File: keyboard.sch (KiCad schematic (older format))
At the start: 16 parts, among them SW1 SW_Push, U1 ATmega32U4-AU, Y1 16MHz

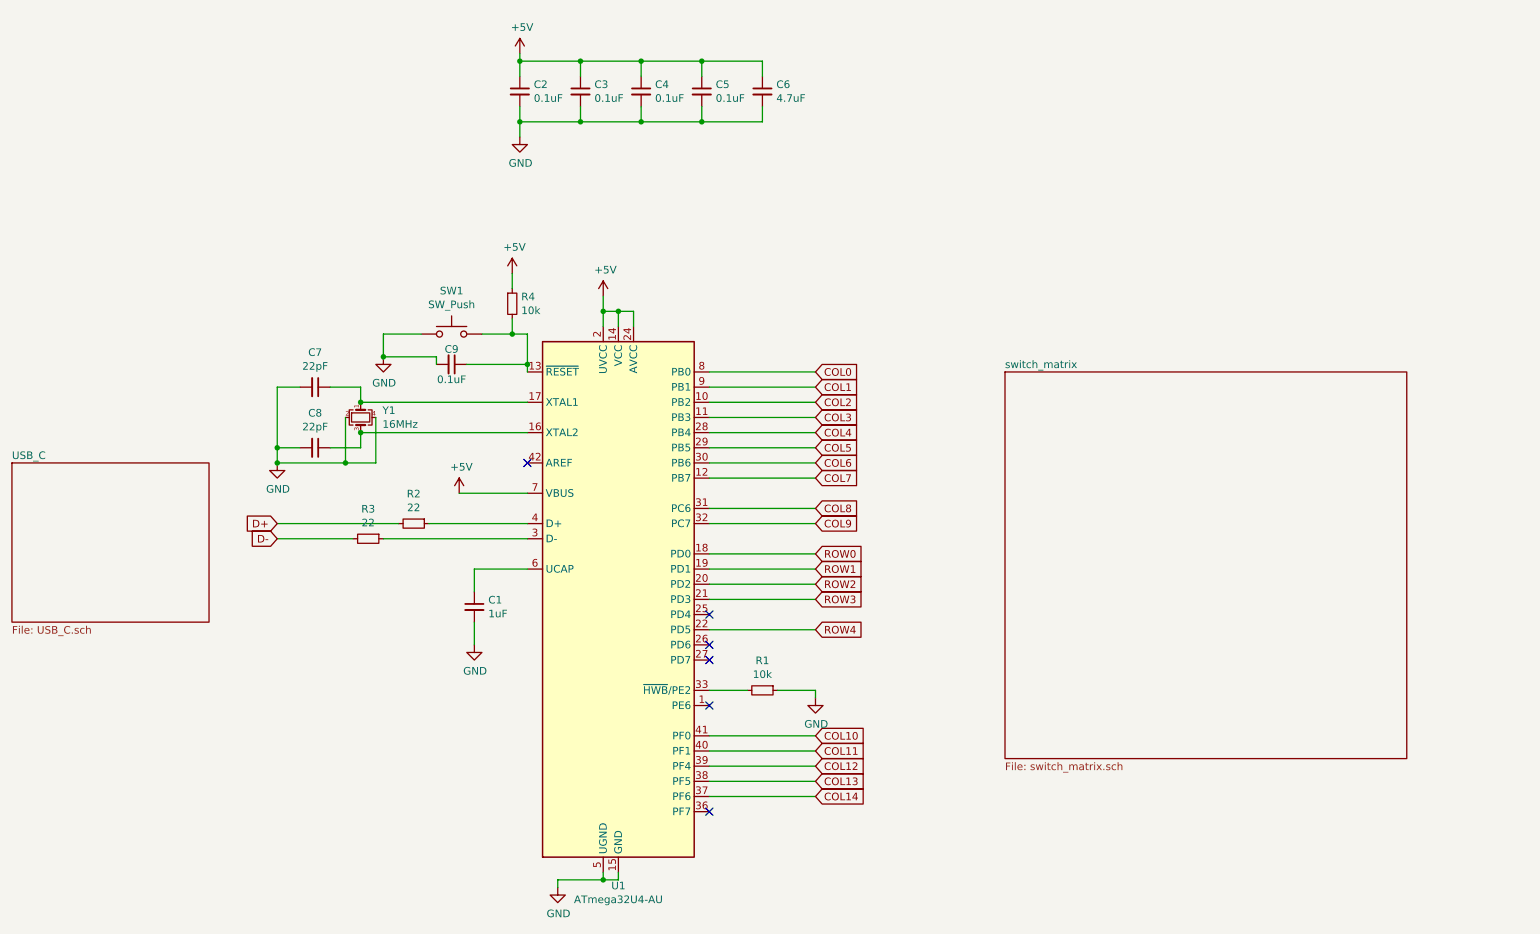
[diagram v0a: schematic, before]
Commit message: Assigned footprint
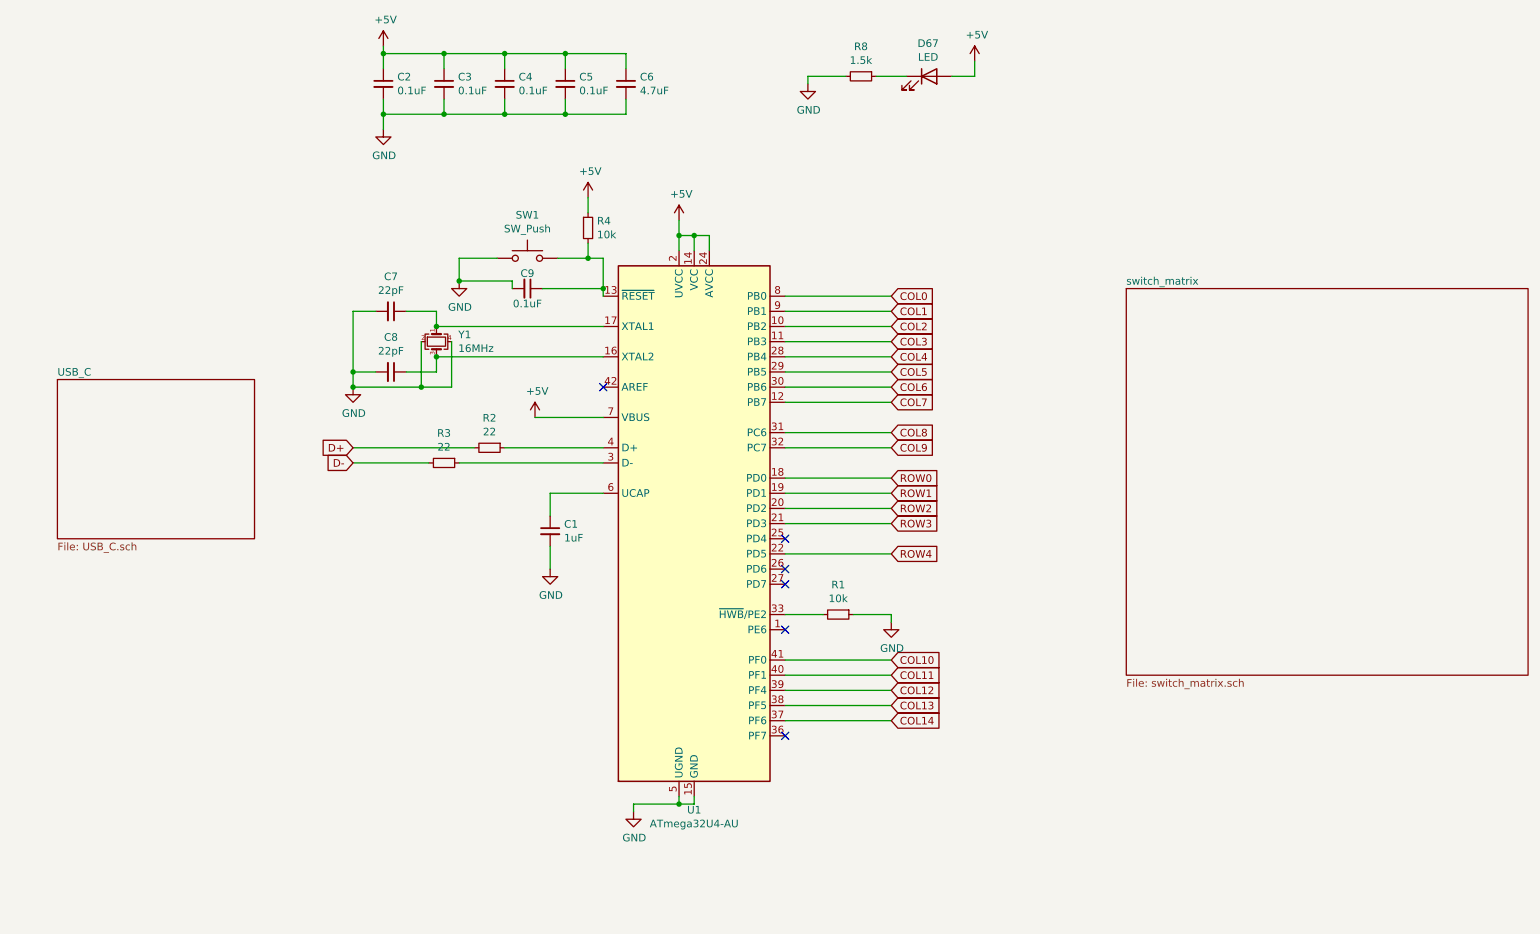
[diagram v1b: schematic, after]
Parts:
- added D67: LED, LED_SMD:LED_0805_2012Metric, symbol Device:LED
- added R8: 1.5k, Resistor_SMD:R_0805_2012Metric, symbol Device:R_Small
- C1, C2, C3, C4, C5, C6, C7, C8, C9: footprint (none) -> Capacitor_SMD:C_0805_2012Metric
- R1, R2, R3, R4: footprint (none) -> Resistor_SMD:R_0805_2012Metric
- SW1: footprint (none) -> random-keyboard-parts:SKQG-1155865
- Y1: footprint (none) -> Crystal:Crystal_SMD_3225-4Pin_3.2x2.5mm
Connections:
- net +5V: now also D67.2 (A)
- net GND: now also R8.2
- new net: D67.1 (K), R8.1
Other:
- moved on the sheet: C1, C2, C3, C4, C5, C6, C7, C8, C9, R1, R2, R3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

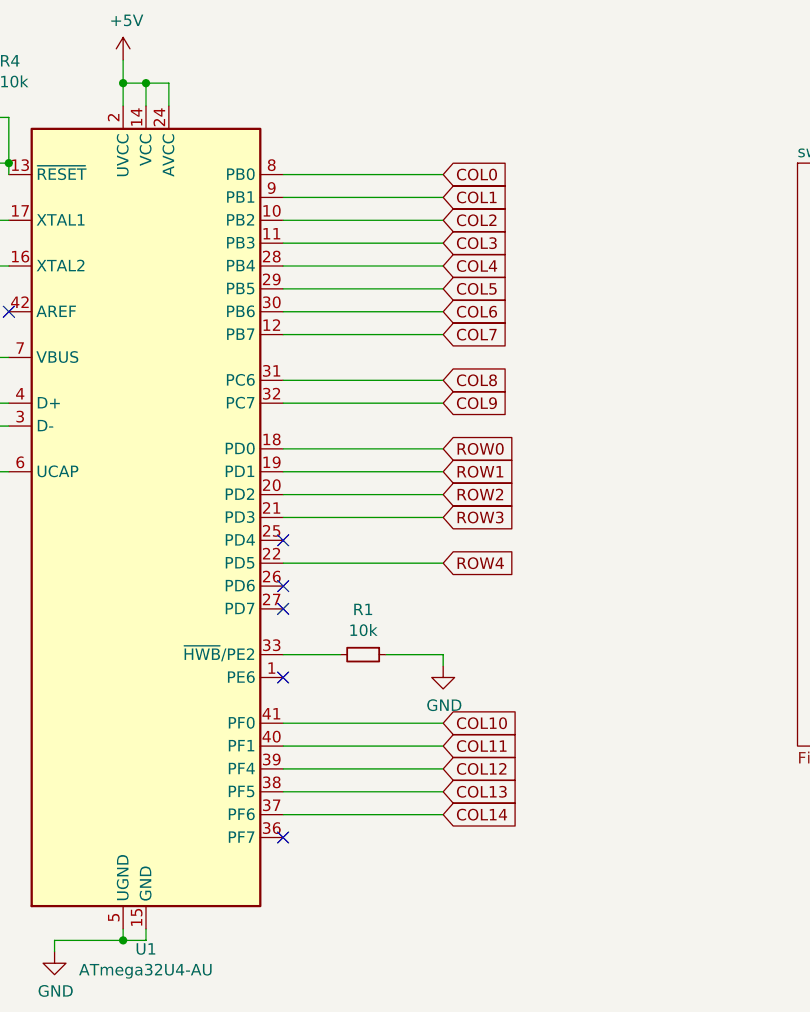
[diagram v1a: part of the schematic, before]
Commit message: Finished routing, filled in ground planes, checked with DRC and 3D render
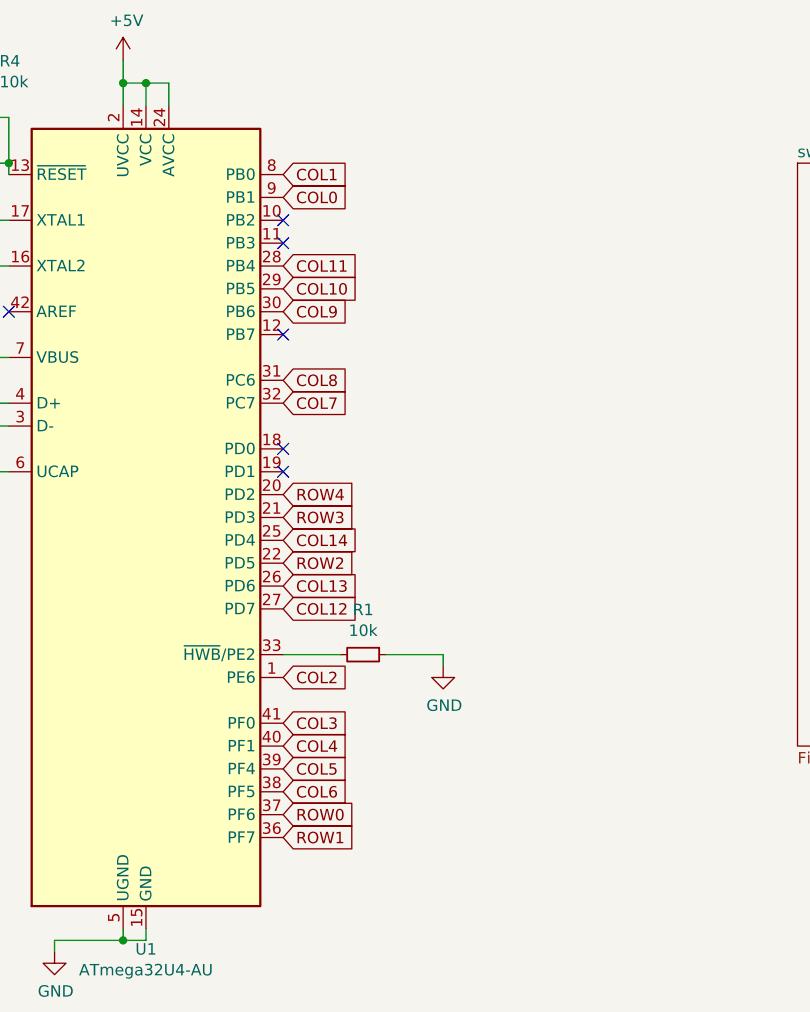
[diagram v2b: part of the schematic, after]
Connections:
- net COL0: now also U1.9 (PB1); no longer U1.8 (PB0)
- net COL1: now also U1.8 (PB0); no longer U1.9 (PB1)
- net COL10: now also U1.29 (PB5); no longer U1.41 (PF0)
- net COL11: now also U1.28 (PB4); no longer U1.40 (PF1)
- net COL12: now also U1.27 (PD7); no longer U1.39 (PF4)
- net COL13: now also U1.26 (PD6); no longer U1.38 (PF5)
- net COL14: now also U1.25 (PD4); no longer U1.37 (PF6)
- net COL2: now also U1.1 (PE6); no longer U1.10 (PB2)
- net COL3: now also U1.41 (PF0); no longer U1.11 (PB3)
- net COL4: now also U1.40 (PF1); no longer U1.28 (PB4)
- net COL5: now also U1.39 (PF4); no longer U1.29 (PB5)
- net COL6: now also U1.38 (PF5); no longer U1.30 (PB6)
- net COL7: now also U1.32 (PC7); no longer U1.12 (PB7)
- net COL9: now also U1.30 (PB6); no longer U1.32 (PC7)
- net ROW0: now also U1.37 (PF6); no longer U1.18 (PD0)
- net ROW1: now also U1.36 (PF7); no longer U1.19 (PD1)
- net ROW2: now also U1.22 (PD5); no longer U1.20 (PD2)
- net ROW4: now also U1.20 (PD2); no longer U1.22 (PD5)
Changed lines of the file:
@@
 	5350 2250 5350 2350
 Connection ~ 5250 2250
-Wire Wire Line
-	5850 3850 6550 3850
-Wire Wire Line
-	5850 3950 6550 3950
-Wire Wire Line
-	5850 4050 6550 4050
-Wire Wire Line
-	5850 4150 6550 4150
-Wire Wire Line
-	5850 4350 6550 4350
-Text GLabel 6550 3850 2    50   Input ~ 0
+Text GLabel 5850 5450 2    50   Input ~ 0
 ROW0
-Text GLabel 6550 3950 2    50   Input ~ 0
+Text GLabel 5850 5550 2    50   Input ~ 0
 ROW1
-Text GLabel 6550 4050 2    50   Input ~ 0
+Text GLabel 5850 4350 2    50   Input ~ 0
 ROW2
-Text GLabel 6550 4150 2    50   Input ~ 0
+Text GLabel 5850 4150 2    50   Input ~ 0
 ROW3
-Text GLabel 6550 4350 2    50   Input ~ 0
+Text GLabel 5850 4050 2    50   Input ~ 0
 ROW4
-Wire Wire Line
-	5850 2650 6550 2650
-Wire Wire Line
-	5850 2750 6550 2750
-Wire Wire Line
-	5850 2850 6550 2850
-Wire Wire Line
-	5850 2950 6550 2950
-Wire Wire Line
-	5850 3050 6550 3050
-Wire Wire Line
-	5850 3150 6550 3150
-Wire Wire Line
-	5850 3250 6550 3250
-Wire Wire Line
-	5850 3350 6550 3350
-Wire Wire Line
-	5850 3550 6550 3550
-Wire Wire Line
-	5850 3650 6550 3650
-Wire Wire Line
-	5850 5050 6550 5050
-Wire Wire Line
-	5850 5150 6550 5150
-Wire Wire Line
-	5850 5250 6550 5250
-Wire Wire Line
-	5850 5350 6550 5350
-Wire Wire Line
-	5850 5450 6550 5450
-NoConn ~ 5850 5550
-NoConn ~ 5850 4250
-NoConn ~ 5850 4550
-NoConn ~ 5850 4450
-NoConn ~ 5850 4850
-Text GLabel 6550 2650 2    50   Input ~ 0
-COL0
-Text GLabel 6550 2750 2    50   Input ~ 0
+Text GLabel 5850 2650 2    50   Input ~ 0
 COL1
-Text GLabel 6550 2850 2    50   Input ~ 0
+Text GLabel 5850 4850 2    50   Input ~ 0
 COL2
-Text GLabel 6550 2950 2    50   Input ~ 0
+Text GLabel 5850 5050 2    50   Input ~ 0
 COL3
-Text GLabel 6550 3050 2    50   Input ~ 0
+Text GLabel 5850 5150 2    50   Input ~ 0
 COL4
-Text GLabel 6550 3150 2    50   Input ~ 0
+Text GLabel 5850 5250 2    50   Input ~ 0
 COL5
-Text GLabel 6550 3250 2    50   Input ~ 0
+Text GLabel 5850 5350 2    50   Input ~ 0
 COL6
-Text GLabel 6550 3350 2    50   Input ~ 0
+Text GLabel 5850 3650 2    50   Input ~ 0
 COL7
-Text GLabel 6550 3550 2    50   Input ~ 0
+Text GLabel 5850 3550 2    50   Input ~ 0
 COL8
-Text GLabel 6550 3650 2    50   Input ~ 0
+Text GLabel 5850 3250 2    50   Input ~ 0
 COL9
-Text GLabel 6550 5050 2    50   Input ~ 0
+Text GLabel 5850 3150 2    50   Input ~ 0
 COL10
-Text GLabel 6550 5150 2    50   Input ~ 0
+Text GLabel 5850 3050 2    50   Input ~ 0
 COL11
-Text GLabel 6550 5250 2    50   Input ~ 0
+Text GLabel 5850 4550 2    50   Input ~ 0
 COL12
-Text GLabel 6550 5350 2    50   Input ~ 0
+Text GLabel 5850 4450 2    50   Input ~ 0
 COL13
-Text GLabel 6550 5450 2    50   Input ~ 0
+Text GLabel 5850 4250 2    50   Input ~ 0
 COL14
 $Sheet
@@
 Wire Wire Line
 	7100 1200 7100 1100
+NoConn ~ 5850 2850
+NoConn ~ 5850 2950
+Text GLabel 5850 2750 2    50   Input ~ 0
+COL0
+NoConn ~ 5850 3350
+NoConn ~ 5850 3850
+NoConn ~ 5850 3950
 $EndSCHEMATC
